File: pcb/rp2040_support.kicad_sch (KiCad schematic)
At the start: 18 parts, among them J3 Debug (JST SH), J4 Debug (2.54mm holes), J5 UJ20-C-H-C-4-SMT-TR, U1 NCP1117-3.3_SOT223, U2 W25Q128JVS, U4 R-667995, Y1 ABM8-272-T3

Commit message: Update the schematic to properly use hierarchical sheets, update the PCB to match, tidy up some weirdnesses (button with a "U" refdes, both S and SW refdes, etc)
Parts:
- renumbered C2 to C3, U4 to S3

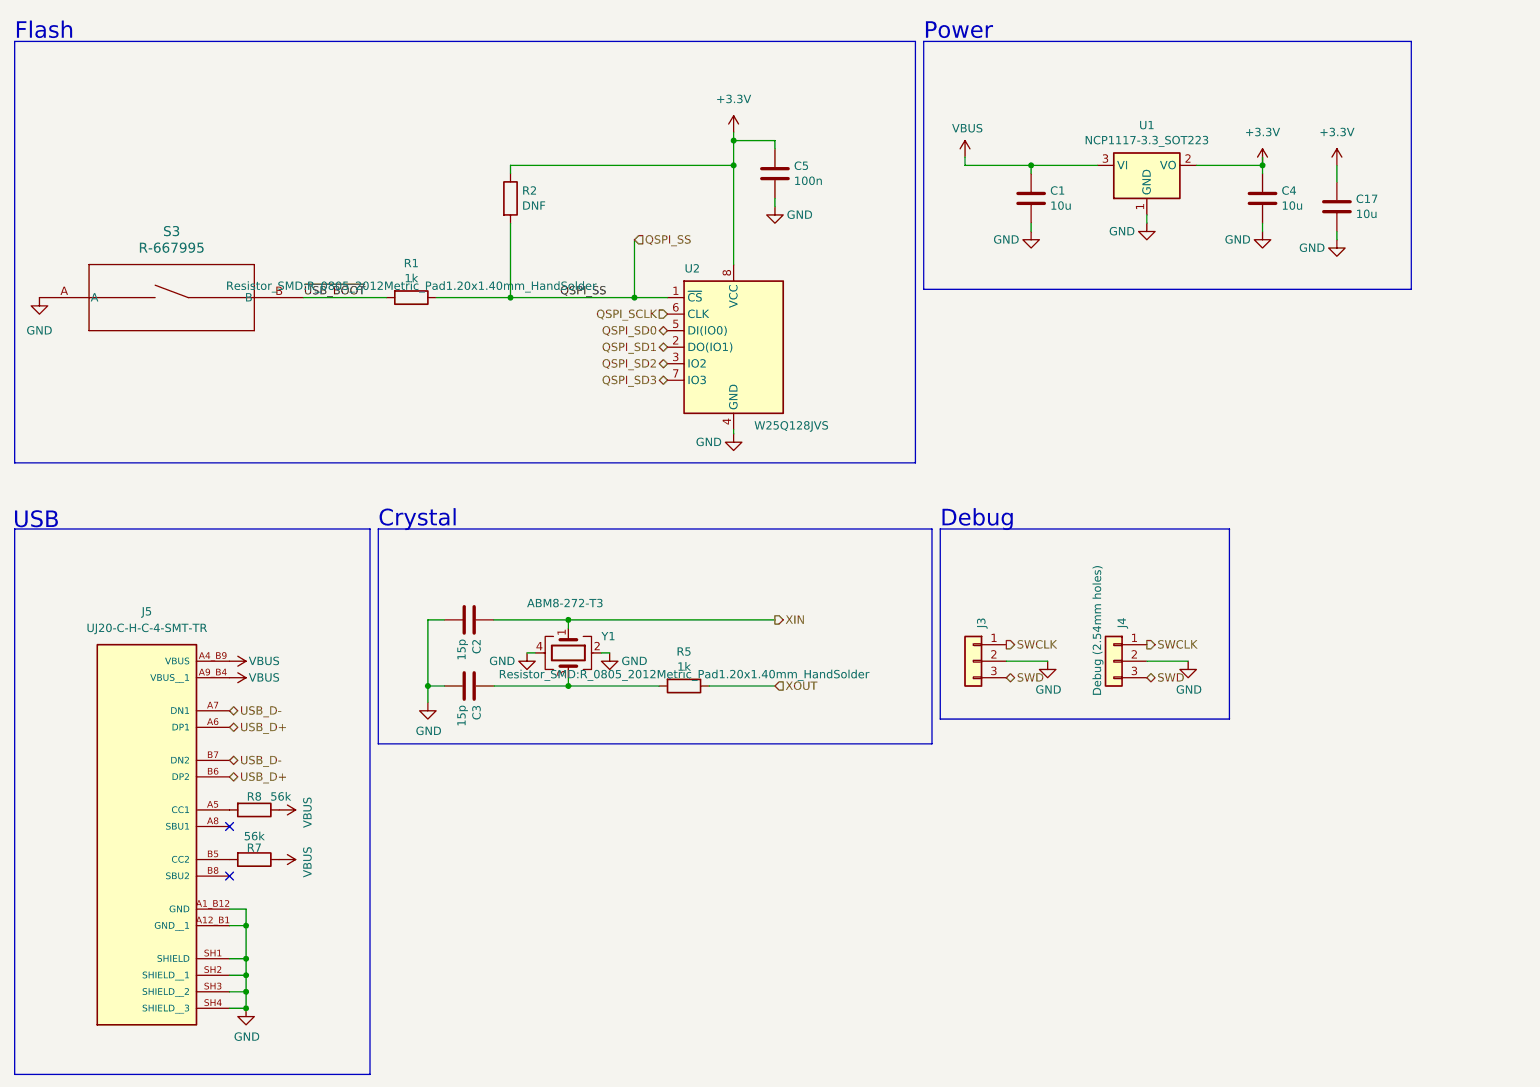
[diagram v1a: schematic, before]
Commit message: Update PCB to v1.1:  * Update level shifting to a component that actually supports 5V  * Make both D-Sub connectors the same size in terms of pin offset (added bonus of making the board smaller)  * Update a couple of footprints that have changed name  * Add a switch for USB host/device,
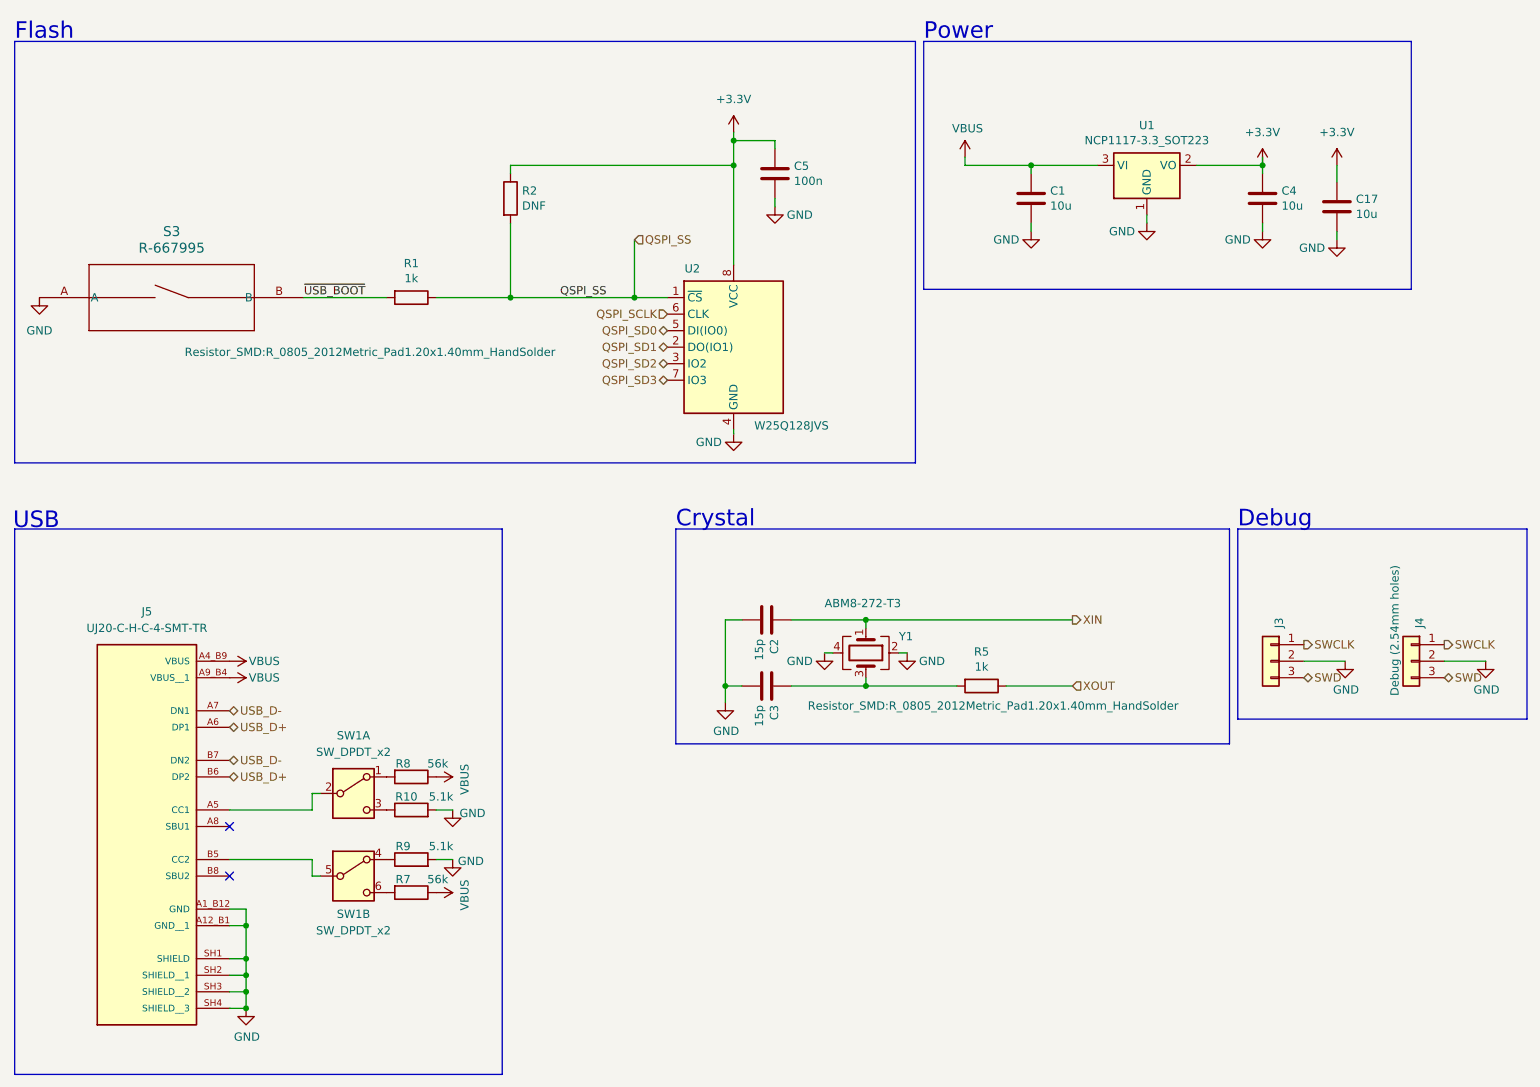
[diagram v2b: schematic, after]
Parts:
- added R10, R9: 5.1k, Resistor_SMD:R_0805_2012Metric_Pad1.20x1.40mm_HandSolder, symbol Device:R
- added SW1: SW_DPDT_x2, Button_Switch_THT:SW_CK_JS202011CQN_DPDT_Straight, symbol Switch:SW_DPDT_x2
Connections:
- net GND: now also R10.2, R9.2
- net at R8.2: now also SW1.1 (A); no longer J5.A5 (CC1)
- net at J5.B5 (CC2): now also SW1.5 (B); no longer R7.2
- new net: R9.1, SW1.4 (A)
- new net: R7.2, SW1.6 (C)
- new net: R10.1, SW1.3 (C)
- new net: J5.A5 (CC1), SW1.2 (B)
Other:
- moved on the sheet: C2, C3, J3, J4, R5, R7, R8, Y1
